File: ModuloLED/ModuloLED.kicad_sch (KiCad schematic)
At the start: 4 parts, among them J23 Pin

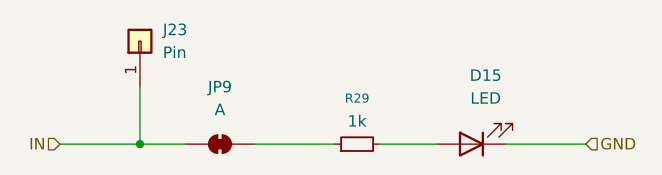
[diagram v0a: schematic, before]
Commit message: Added all components to arduino pcb.
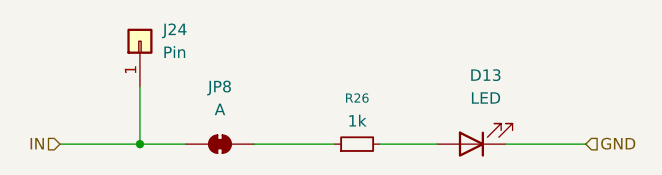
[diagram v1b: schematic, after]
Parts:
- R26: renamed from R29; footprint Resistor_SMD:R_0805_2012Metric -> Resistor_SMD:R_0805_2012Metric_Pad1.20x1.40mm_HandSolder
- renumbered D15 to D13, J23 to J24, JP9 to JP8
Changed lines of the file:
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@@
 		(dnp no)
 		(fields_autoplaced yes)
-		(property "Reference" "D15"
+		(property "Reference" "D13"
 			(at 120.9675 78.74 0)
 			(effects
@@
 			(project "Arduino"
 				(path "/b1260de1-9c48-4b08-a759-f31e40d6183e/54e8ff50-b2bf-453b-97e6-5b05d2e40d47"
-					(reference "D16")
-					(unit 1)
-				)
-				(path "/b1260de1-9c48-4b08-a759-f31e40d6183e/c9e917bf-8660-4cf1-93f8-b84cf07b2025"
-					(reference "D15")
+					(reference "D14")
+					(unit 1)
+				)
+				(path "/b1260de1-9c48-4b08-a759-f31e40d6183e/c9e917bf-8660-4cf1-93f8-b84cf07b2025"
+					(reference "D13")
 					(unit 1)
 				)
@@
 		(dnp no)
 		(fields_autoplaced yes)
-		(property "Reference" "JP9"
+		(property "Reference" "JP8"
 			(at 91.44 80.01 0)
 			(effects
@@
 			(project "Arduino"
 				(path "/b1260de1-9c48-4b08-a759-f31e40d6183e/54e8ff50-b2bf-453b-97e6-5b05d2e40d47"
-					(reference "JP10")
-					(unit 1)
-				)
-				(path "/b1260de1-9c48-4b08-a759-f31e40d6183e/c9e917bf-8660-4cf1-93f8-b84cf07b2025"
 					(reference "JP9")
+					(unit 1)
+				)
+				(path "/b1260de1-9c48-4b08-a759-f31e40d6183e/c9e917bf-8660-4cf1-93f8-b84cf07b2025"
+					(reference "JP8")
 					(unit 1)
 				)
@@
 		(dnp no)
 		(fields_autoplaced yes)
-		(property "Reference" "R29"
+		(property "Reference" "R26"
 			(at 106.68 81.28 90)
 			(effects
@@
 			)
 		)
-		(property "Footprint" "Resistor_SMD:R_0805_2012Metric"
+		(property "Footprint" "Resistor_SMD:R_0805_2012Metric_Pad1.20x1.40mm_HandSolder"
 			(at 106.68 86.36 0)
 			(effects
@@
 			(project "Arduino"
 				(path "/b1260de1-9c48-4b08-a759-f31e40d6183e/54e8ff50-b2bf-453b-97e6-5b05d2e40d47"
-					(reference "R30")
-					(unit 1)
-				)
-				(path "/b1260de1-9c48-4b08-a759-f31e40d6183e/c9e917bf-8660-4cf1-93f8-b84cf07b2025"
-					(reference "R29")
+					(reference "R27")
+					(unit 1)
+				)
+				(path "/b1260de1-9c48-4b08-a759-f31e40d6183e/c9e917bf-8660-4cf1-93f8-b84cf07b2025"
+					(reference "R26")
 					(unit 1)
 				)
@@
 		(dnp no)
 		(fields_autoplaced yes)
-		(property "Reference" "J23"
+		(property "Reference" "J24"
 			(at 85.09 73.6599 90)
 			(effects
@@
 			(project "Arduino"
 				(path "/b1260de1-9c48-4b08-a759-f31e40d6183e/54e8ff50-b2bf-453b-97e6-5b05d2e40d47"
+					(reference "J25")
+					(unit 1)
+				)
+				(path "/b1260de1-9c48-4b08-a759-f31e40d6183e/c9e917bf-8660-4cf1-93f8-b84cf07b2025"
 					(reference "J24")
 					(unit 1)
 				)
-				(path "/b1260de1-9c48-4b08-a759-f31e40d6183e/c9e917bf-8660-4cf1-93f8-b84cf07b2025"
-					(reference "J23")
-					(unit 1)
-				)

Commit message: First version from PCB schematic.
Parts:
- renumbered JP8 to JP9
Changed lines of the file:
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@@
 		(dnp no)
 		(fields_autoplaced yes)
-		(property "Reference" "JP8"
+		(property "Reference" "JP9"
 			(at 91.44 80.01 0)
 			(effects
@@
 			(project "Arduino"
 				(path "/b1260de1-9c48-4b08-a759-f31e40d6183e/54e8ff50-b2bf-453b-97e6-5b05d2e40d47"
+					(reference "JP10")
+					(unit 1)
+				)
+				(path "/b1260de1-9c48-4b08-a759-f31e40d6183e/c9e917bf-8660-4cf1-93f8-b84cf07b2025"
 					(reference "JP9")
 					(unit 1)
 				)
-				(path "/b1260de1-9c48-4b08-a759-f31e40d6183e/c9e917bf-8660-4cf1-93f8-b84cf07b2025"
-					(reference "JP8")
-					(unit 1)
-				)
